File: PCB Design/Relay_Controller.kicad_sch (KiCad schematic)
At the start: 58 parts, among them J1 Mains, J11 Conn_Aux, J12 Conn_Sig, J13 Conn_I2C, J14 Conn_I2C, J15 Conn_01x04_Pin, J2 Conn_IO, J3 Conn_IO11, J4 Conn_IO12, J41 Conn_01x03_Pin, U11 AMS1117-3.3, U12 SX1509BIULTRT, U13 TCA9406DC

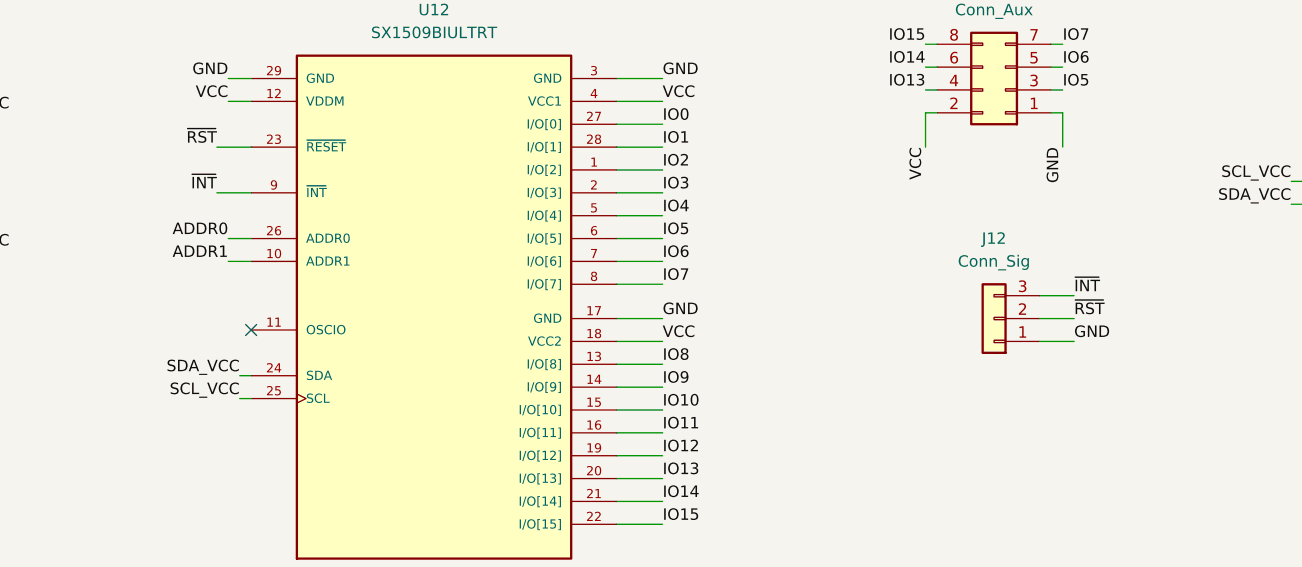
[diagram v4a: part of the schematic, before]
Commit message: Add OSCIO pin and voltage section silk-screen
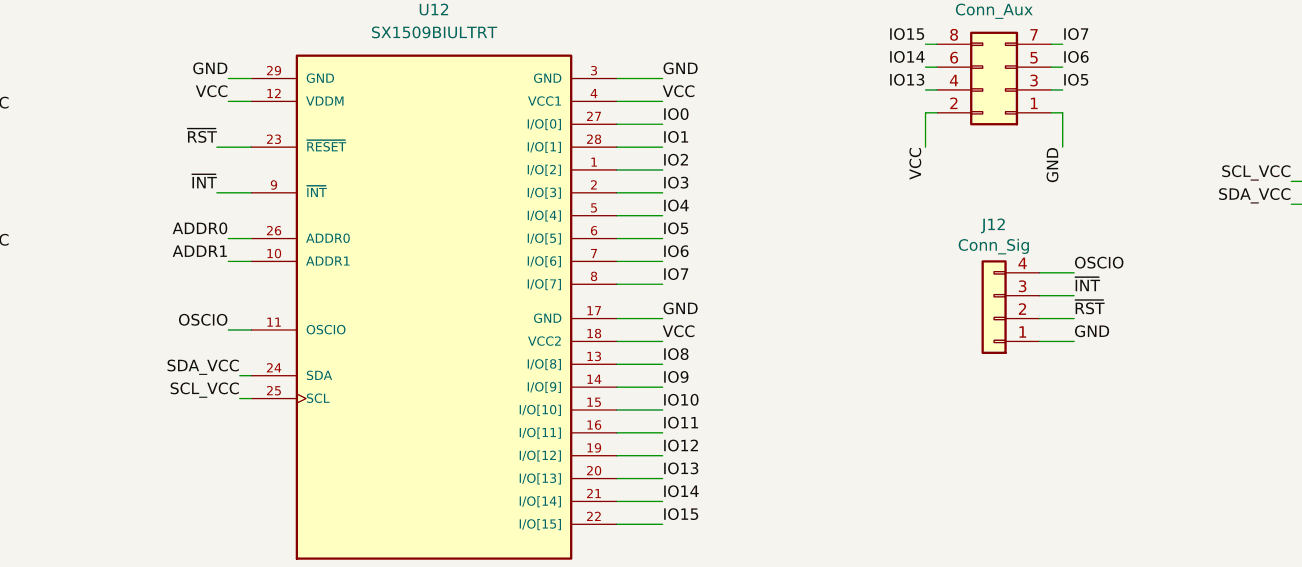
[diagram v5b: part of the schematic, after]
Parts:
- J12: footprint Connector_JST:JST_XH_B3B-XH-A_1x03_P2.50mm_Vertical -> Connector_JST:JST_XH_B4B-XH-A_1x04_P2.50mm_Vertical; symbol Connector_Generic:Conn_01x03 -> Connector_Generic:Conn_01x04
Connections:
- net OSCIO: now reaches U12.11 (OSCIO)
- net OSCIO: now also J12.4 (Pin_4)
- no-connect marks 1 -> 0
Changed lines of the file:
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@@
 		(color 0 0 0 0)
 	)
-	(no_connect
-		(at 77.47 151.13)
-	)
 	(wire
 		(pts
@@
 	(wire
 		(pts
-			(xy 165.1 149.86) (xy 168.91 149.86)
+			(xy 165.1 144.78) (xy 168.91 144.78)
 		)
 		(stroke
@@
 	(wire
 		(pts
-			(xy 165.1 147.32) (xy 168.91 147.32)
-		)
-		(stroke
-			(width 0)
-			(type default)
-		)
-	)
-	(wire
-		(pts
 			(xy 203.2 76.2) (xy 203.2 78.74)
 		)
@@
 	(wire
 		(pts
+			(xy 74.93 151.13) (xy 77.47 151.13)
+		)
+		(stroke
+			(width 0)
+			(type default)
+		)
+	)
+	(wire
+		(pts
 			(xy 171.45 30.48) (xy 171.45 35.56)
 		)
@@
 	(wire
 		(pts
+			(xy 165.1 147.32) (xy 168.91 147.32)
+		)
+		(stroke
+			(width 0)
+			(type default)
+		)
+	)
+	(wire
+		(pts
 			(xy 87.63 101.6) (xy 90.17 101.6)
 		)
@@
 	(wire
 		(pts
+			(xy 165.1 149.86) (xy 168.91 149.86)
+		)
+		(stroke
+			(width 0)
+			(type default)
+		)
+	)
+	(wire
+		(pts
 			(xy 27.94 96.52) (xy 30.48 96.52)
 		)
@@
 		)
 	)
+	(label "OSCIO"
+		(at 168.91 144.78 0)
+		(fields_autoplaced yes)
+		(effects
+			(font
+				(size 1.27 1.27)
+			)
+			(justify left bottom)
+		)
+	)
 	(label "GND"
 		(at 31.75 127 180)
@@
 		)
 	)
+	(label "OSCIO"
+		(at 74.93 151.13 180)
+		(fields_autoplaced yes)
+		(effects
+			(font
+				(size 1.27 1.27)
+			)
+			(justify right bottom)
+		)
+	)
 	(label "+5V"
 		(at 90.17 69.85 180)
@@
 		)
 	)
+	(label "~{INT}"
+		(at 168.91 147.32 0)
+		(fields_autoplaced yes)
+		(effects
+			(font
+				(size 1.27 1.27)
+			)
+			(justify left bottom)
+		)
+	)
 	(label "IO14"
 		(at 152.4 121.92 180)
@@
 		)
 	)
+	(label "~{RST}"
+		(at 168.91 149.86 0)
+		(fields_autoplaced yes)
+		(effects
+			(font
+				(size 1.27 1.27)
+			)
+			(justify left bottom)
+		)
+	)
 	(label "SCL"
 		(at 246.38 149.86 180)
@@
 		)
 	)
-	(label "~{INT}"
-		(at 168.91 147.32 0)
-		(fields_autoplaced yes)
-		(effects
-			(font
-				(size 1.27 1.27)
-			)
-			(justify left bottom)
-		)
-	)
 	(label "IO5"
 		(at 123.19 140.97 0)
@@
 		)
 	)
-	(label "~{RST}"
-		(at 168.91 149.86 0)
-		(fields_autoplaced yes)
-		(effects
-			(font
-				(size 1.27 1.27)
-			)
-			(justify left bottom)
-		)
-	)
 	(hierarchical_label "AC_Neut"
 		(shape input)
@@
 	)
 	(symbol
-		(lib_id "Connector_Generic:Conn_01x03")
+		(lib_id "Connector_Generic:Conn_01x04")
 		(at 160.02 149.86 180)
 		(unit 1)
@@
 		(dnp no)
 		(property "Reference" "J12"
-			(at 160.02 140.97 0)
+			(at 160.02 139.446 0)
 			(effects
 				(font
@@
 		)
 		(property "Value" "Conn_Sig"
-			(at 160.02 143.51 0)
+			(at 160.02 141.732 0)
 			(effects
 				(font
@@
 			)
 		)
-		(property "Footprint" "Connector_JST:JST_XH_B3B-XH-A_1x03_P2.50mm_Vertical"
+		(property "Footprint" "Connector_JST:JST_XH_B4B-XH-A_1x04_P2.50mm_Vertical"
 			(at 160.02 149.86 0)
 			(effects
@@
 			)
 		)
-		(property "Description" "Generic connector, single row, 01x03, script generated (kicad-library-utils/schlib/autogen/connector/)"
+		(property "Description" "Generic connector, single row, 01x04, script generated (kicad-library-utils/schlib/autogen/connector/)"
 			(at 160.02 149.86 0)
 			(effects
@@
 		(pin "3"
 		)
+		(pin "4"
+		)
 		(instances

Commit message: Testpoints to schematic.
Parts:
- added C13: 0.1uF, Capacitor_SMD:C_0805_2012Metric_Pad1.18x1.45mm_HandSolder, symbol Device:C_Small
- added TP11: IO2, Footprints:TestPoint_Pad_D1.0mm, symbol Connector:TestPoint_Small
- added TP12: IO3, Footprints:TestPoint_Pad_D1.0mm, symbol Connector:TestPoint_Small
- added TP13, TP21, TP28, TP67: VCC, Footprints:TestPoint_Pad_D1.0mm, symbol Connector:TestPoint_Small
- added TP14, TP22, TP68: GND, Footprints:TestPoint_Pad_D1.0mm, symbol Connector:TestPoint_Small
- added TP15: IO4, Footprints:TestPoint_Pad_D1.0mm, symbol Connector:TestPoint_Small
- added TP16: IO5, Footprints:TestPoint_Pad_D1.0mm, symbol Connector:TestPoint_Small
- added TP17: IO6, Footprints:TestPoint_Pad_D1.0mm, symbol Connector:TestPoint_Small
- added TP18: IO7, Footprints:TestPoint_Pad_D1.0mm, symbol Connector:TestPoint_Small
- added TP19: ~{INT}, Footprints:TestPoint_Pad_D1.0mm, symbol Connector:TestPoint_Small
- added TP20: ~{RST}, Footprints:TestPoint_Pad_D1.0mm, symbol Connector:TestPoint_Small
- added TP23: Addr0, Footprints:TestPoint_Pad_D1.0mm, symbol Connector:TestPoint_Small
- added TP24: Addr1, Footprints:TestPoint_Pad_D1.0mm, symbol Connector:TestPoint_Small
- added TP25: OSC, Footprints:TestPoint_Pad_D1.0mm, symbol Connector:TestPoint_Small
- added TP26: SDA, Footprints:TestPoint_Pad_D1.0mm, symbol Connector:TestPoint_Small
- added TP27: SCL, Footprints:TestPoint_Pad_D1.0mm, symbol Connector:TestPoint_Small
- added TP29: IO8, Footprints:TestPoint_Pad_D1.0mm, symbol Connector:TestPoint_Small
- added TP30: IO9, Footprints:TestPoint_Pad_D1.0mm, symbol Connector:TestPoint_Small
- added TP31: IO10, Footprints:TestPoint_Pad_D1.0mm, symbol Connector:TestPoint_Small
- added TP32: IO11, Footprints:TestPoint_Pad_D1.0mm, symbol Connector:TestPoint_Small
- added TP33: IO12, Footprints:TestPoint_Pad_D1.0mm, symbol Connector:TestPoint_Small
- added TP34: IO13, Footprints:TestPoint_Pad_D1.0mm, symbol Connector:TestPoint_Small
- added TP35: IO14, Footprints:TestPoint_Pad_D1.0mm, symbol Connector:TestPoint_Small
- added TP36: IO15, Footprints:TestPoint_Pad_D1.0mm, symbol Connector:TestPoint_Small
- added TP37: IO0, Footprints:TestPoint_Pad_D1.0mm, symbol Connector:TestPoint_Small
- added TP38: IO1, Footprints:TestPoint_Pad_D1.0mm, symbol Connector:TestPoint_Small
- added TP69: 5V, Footprints:TestPoint_Pad_D1.0mm, symbol Connector:TestPoint_Small
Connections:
- net +5V: now also C13.1, TP69.1
- net ADDR0: now also TP23.1
- net ADDR1: now also TP24.1
- net GND: now also C13.2, TP14.1, TP22.1, TP68.1
- net IO0: now also TP37.1
- net IO1: now also TP38.1
- net IO10: now also TP31.1
- net IO11: now also TP32.1
- net IO12: now also TP33.1
- net IO13: now also TP34.1
- net IO14: now also TP35.1
- net IO15: now also TP36.1
- net IO2: now also TP11.1
- net IO3: now also TP12.1
- net IO4: now also TP15.1
- net IO5: now also TP16.1
- net IO6: now also TP17.1
- net IO7: now also TP18.1
- net IO8: now also TP29.1
- net IO9: now also TP30.1
- net OSCIO: now also TP25.1
- net SCL_VCC: now also TP27.1
- net SDA_VCC: now also TP26.1
- net VCC: now also TP13.1, TP21.1, TP28.1, TP67.1
- net ~{INT}: now also TP19.1
- net ~{RST}: now also TP20.1

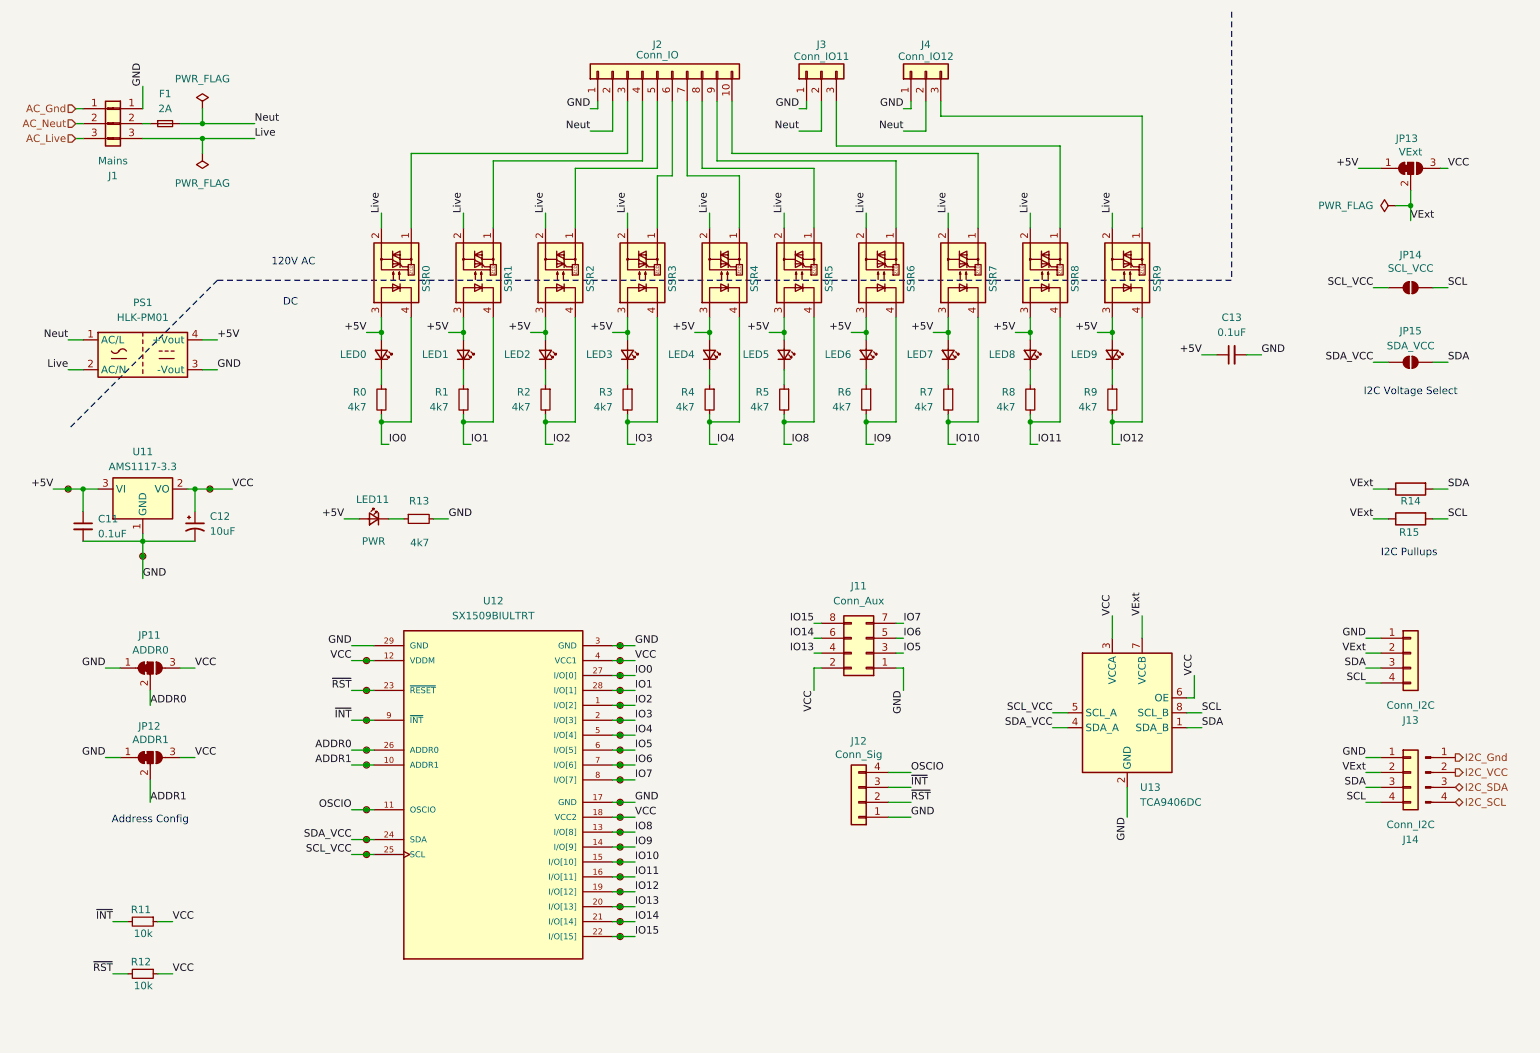
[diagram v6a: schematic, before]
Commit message: Vcc->3v3 Added extra GPIO
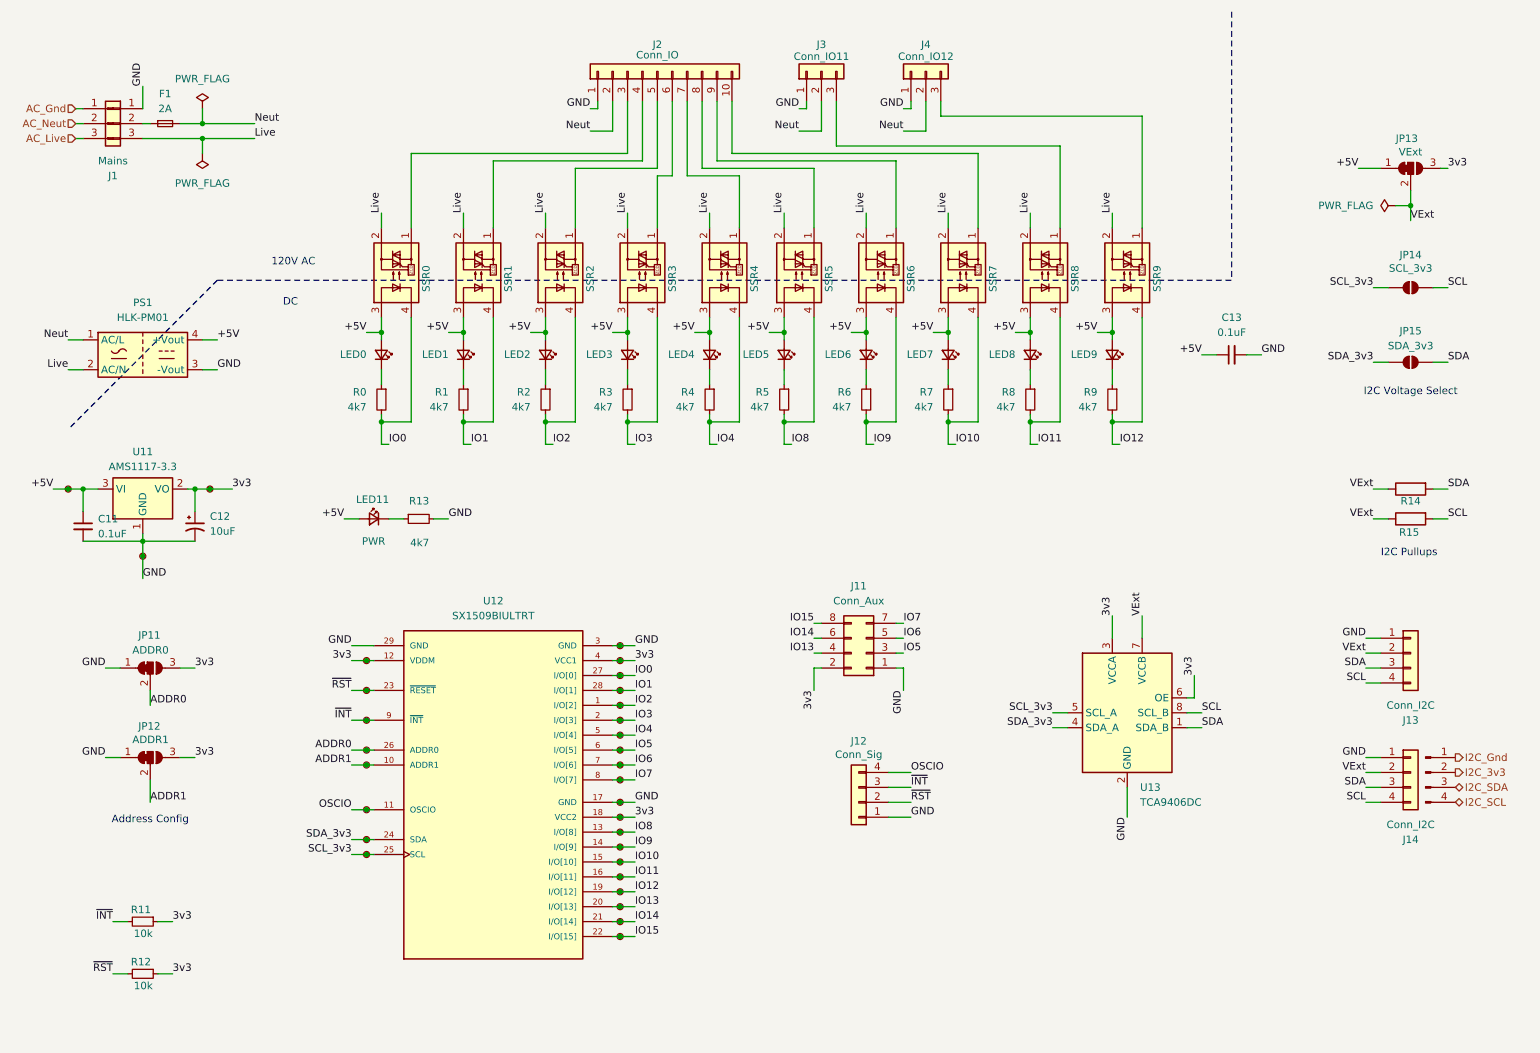
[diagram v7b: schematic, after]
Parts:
- JP14: value SCL_VCC -> SCL_3v3
- JP15: value SDA_VCC -> SDA_3v3
- TP13, TP21, TP28, TP67: value VCC -> 3v3
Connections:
- net I2C_VCC renamed I2C_3v3
- net SCL_VCC renamed SCL_3v3
- net SDA_VCC renamed SDA_3v3
- net VCC renamed 3v3
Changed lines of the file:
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@@
 		)
 	)
-	(label "VCC"
+	(label "3v3"
 		(at 43.18 179.07 0)
 		(fields_autoplaced yes)
@@
 		)
 	)
-	(label "SCL_VCC"
+	(label "SCL_3v3"
 		(at 247.65 62.23 180)
 		(fields_autoplaced yes)
@@
 		)
 	)
-	(label "VCC"
+	(label "3v3"
 		(at 46.99 127 0)
 		(fields_autoplaced yes)
@@
 		)
 	)
-	(label "VCC"
+	(label "3v3"
 		(at 217.17 128.27 90)
 		(fields_autoplaced yes)
@@
 		)
 	)
-	(label "VCC"
+	(label "3v3"
 		(at 203.2 118.11 90)
 		(fields_autoplaced yes)
@@
 		)
 	)
-	(label "SDA_VCC"
+	(label "SDA_3v3"
 		(at 193.04 137.16 180)
 		(fields_autoplaced yes)
@@
 		)
 	)
-	(label "VCC"
+	(label "3v3"
 		(at 260.35 41.91 0)
 		(fields_autoplaced yes)
@@
 		)
 	)
-	(label "VCC"
+	(label "3v3"
 		(at 43.18 170.18 0)
 		(fields_autoplaced yes)
@@
 		)
 	)
-	(label "VCC"
+	(label "3v3"
 		(at 73.66 125.73 180)
 		(fields_autoplaced yes)
@@
 		)
 	)
-	(label "VCC"
+	(label "3v3"
 		(at 121.92 125.73 0)
 		(fields_autoplaced yes)
@@
 		)
 	)
-	(label "SDA_VCC"
+	(label "SDA_3v3"
 		(at 73.66 156.21 180)
 		(fields_autoplaced yes)
@@
 		)
 	)
-	(label "VCC"
+	(label "3v3"
 		(at 152.4 130.81 270)
 		(fields_autoplaced yes)
@@
 		)
 	)
-	(label "SCL_VCC"
+	(label "SCL_3v3"
 		(at 193.04 134.62 180)
 		(fields_autoplaced yes)
@@
 		)
 	)
-	(label "SDA_VCC"
+	(label "SDA_3v3"
 		(at 247.65 74.93 180)
 		(fields_autoplaced yes)
@@
 		)
 	)
-	(label "VCC"
+	(label "3v3"
 		(at 46.99 142.24 0)
 		(fields_autoplaced yes)
@@
 		)
 	)
-	(label "SCL_VCC"
+	(label "SCL_3v3"
 		(at 73.66 158.75 180)
 		(fields_autoplaced yes)
@@
 		)
 	)
-	(label "VCC"
+	(label "3v3"
 		(at 121.92 152.4 0)
 		(fields_autoplaced yes)
@@
 		)
 	)
-	(label "VCC"
+	(label "3v3"
 		(at 53.34 96.52 0)
 		(fields_autoplaced yes)
@@
 		)
 	)
-	(hierarchical_label "I2C_VCC"
+	(hierarchical_label "I2C_3v3"
 		(shape output)
 		(at 261.62 144.78 0)
@@
 			)
 		)
-		(property "Value" "SCL_VCC"
+		(property "Value" "SCL_3v3"
 			(at 254 58.928 0)
 			(effects
@@
 			)
 		)
-		(property "Value" "VCC"
+		(property "Value" "3v3"
 			(at 50.8 97.7899 0)
 			(effects
@@
 			)
 		)
-		(property "Value" "VCC"
+		(property "Value" "3v3"
 			(at 120.65 153.6699 0)
 			(effects
@@
 			)
 		)
-		(property "Value" "VCC"
+		(property "Value" "3v3"
 			(at 120.65 126.9999 0)
 			(effects
@@
 			)
 		)
-		(property "Value" "VCC"
+		(property "Value" "3v3"
 			(at 77.47 126.9999 0)
 			(effects
@@
 			)
 		)
-		(property "Value" "SDA_VCC"
+		(property "Value" "SDA_3v3"
 			(at 254 72.136 0)
 			(effects
